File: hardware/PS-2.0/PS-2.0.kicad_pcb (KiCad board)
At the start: 2 copper layers, 119.7 x 199.4 mm, 50 parts, among them J1 PinSocket_02x16_P2.54mm_Verti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, J2 Conn_01x05, J3 Conn_01x05, J8 Conn_01x03, J9 Conn_01x03, K1 RAYEX-L90, K2 RAYEX-L90, Q1 IRFPE50, Q2 IRFPE50, Q3 IRFPE50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

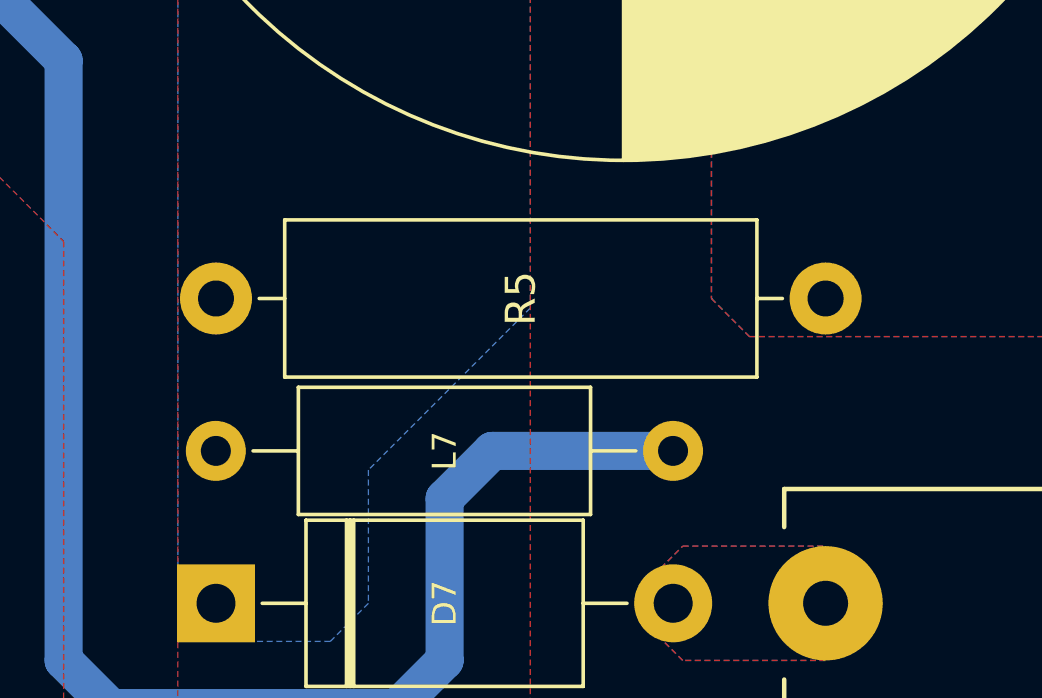
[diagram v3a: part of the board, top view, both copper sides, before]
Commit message: modified:   .DS_Store 	modified:   README.md 	deleted:    hardware/CTL-1.0/CTL-1.0-backups/CTL-1.0-2025-05-23_140814.zip 	deleted:    hardware/CTL-1.0/CTL-1.0-backups/CTL-1.0-2025-05-23_142136.zip 	deleted:    hardware/CTL-1.0/CTL-1.0-backups/CTL-1.0-2025-05-23_145207.zip 	deleted:    hardware/CTL-1.0/CTL-1.0-backups/CTL-1.0-2025-05-23_145749.zip 	deleted:    hardware/CTL-1.0/CTL-1.0-backups/CTL-1.0-2025-06-03_185115.zip 	new file:   hardware/CTL-1.0/CTL-1.0-backups/CTL-1.0-2025-06-04_091843.zip 	new file:   hardware/CTL-1.0/CTL-1.0-backups/CTL-1.0-2025-06-04_105408.zip 	new file:   hardware/CTL-1.0/CTL-1.0-backups/CTL-1.0-2025-06-04_105918.zip 	new file:   hardware/CTL-1.0/CTL-1.0-backups/CTL-1.0-2025-06-04_110436.zip 	new file:   hardware/CTL-1.0/CTL-1.0-backups/CTL-1.0-2025-06-04_115049.zip 	new file:   hardware/CTL-1.0/CTL-1.0-backups/CTL-1.0-2025-06-04_132910.zip 	modified:   hardware/CTL-1.0/CTL-1.0.kicad_pcb 	modified:   hardware/CTL-1.0/CTL-1.0.kicad_prl 	modified:   hardware/CTL-1.0/CTL-1.0.kicad_sch 	new file:   hardware/PS-2.0/PS-2.0-backups/PS-2.0-2025-06-04_100004.zip 	new file:   hardware/PS-2.0/PS-2.0-backups/PS-2.0-2025-06-04_102434.zip 	new file:   hardware/PS-2.0/PS-2.0-backups/PS-2.0-2025-06-04_104734.zip 	new file:   hardware/PS-2.0/PS-2.0-backups/PS-2.0-2025-06-04_133345.zip 	modified:   hardware/PS-2.0/PS-2.0.kicad_pcb 	modified:   hardware/PS-2.0/PS-2.0.kicad_prl 	modified:   hardware/PS-2.0/PS-2.0.kicad_sch 	new file:   hardware/PS-2.0/~PS-2.0.kicad_pcb.lck 	new file:   hardware/PS-2.0/~PS-2.0.kicad_sch.lck 	modified:   pic/.DS_Store 	new file:   pic/PWM/Wave-pure-cut-driver-mosfet.png 	renamed:    pic/PWM/blend-cut-1/blend-cut-1-10.csv -> pic/PWM/blend-cut-1/CTL/blend-cut-1-10.csv 	renamed:    pic/PWM/blend-cut-1/blend-cut-1-10.png -> pic/PWM/blend-cut-1/CTL/blend-cut-1-10.png 	renamed:    pic/PWM/blend-cut-1/blend-cut-1-100.csv -> pic/PWM/blend-cut-1/CTL/blend-cut-1-100.csv 	renamed:    pic/PWM/blend-cut-1/blend-cut-1-100.png -> pic/PWM/ble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
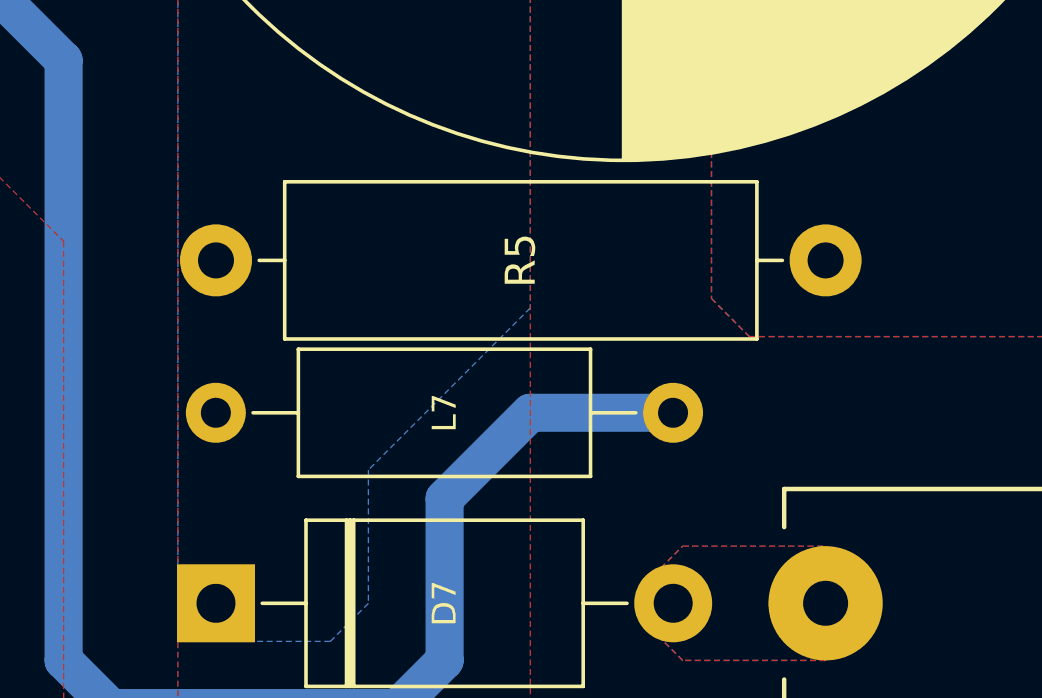
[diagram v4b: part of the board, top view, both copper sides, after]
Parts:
- moved L7 1.27 mm to (208.9, 190.5)
- moved R5 1.27 mm to (229.2, 185.4)
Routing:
- net Net-(C4-Pad1): track 186.0 -> 186.5 mm
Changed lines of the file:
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@@
 	(footprint "Inductor_THT:L_Axial_L9.5mm_D4.0mm_P15.24mm_Horizontal_Fastron_SMCC"
 		(layer "F.Cu")
-		(at 208.91 191.77)
+		(at 208.91 190.5)
 		(descr "Inductor, Axial series, Axial, Horizontal, pin pitch=15.24mm, , length*diameter=9.5*4mm^2, Fastron, SMCC, http://cdn-reichelt.de/documents/datenblatt/B400/DS_SMCC_NEU.pdf, http://cdn-reichelt.de/documents/datenblatt/B400/LEADEDINDUCTORS.pdf")
 		(tags "Inductor Axial series Axial Horizontal pin pitch 15.24mm  length 9.5mm diameter 4mm Fastron SMCC")
@@
 	(footprint "Resistor_THT:R_Axial_DIN0516_L15.5mm_D5.0mm_P20.32mm_Horizontal"
 		(layer "F.Cu")
-		(at 229.235 186.69 180)
+		(at 229.235 185.42 180)
 		(descr "Resistor, Axial_DIN0516 series, Axial, Horizontal, pin pitch=20.32mm, 2W, length*diameter=15.5*5mm^2, http://cdn-reichelt.de/documents/datenblatt/B400/1_4W%23YAG.pdf")
 		(tags "Resistor Axial_DIN0516 series Axial Horizontal pin pitch 20.32mm 2W length 15.5mm diameter 5mm")
@@
 	)
 	(segment
-		(start 205.4225 200.3425)
-		(end 203.835 198.755)
+		(start 216.535 198.755)
+		(end 214.9475 200.3425)
 		(width 1.27)
 		(layer "B.Cu")
@@
 	)
 	(segment
-		(start 196.5325 155.9325)
-		(end 199.7075 152.7575)
+		(start 168.335 126.0475)
+		(end 168.305 126.0775)
 		(width 1.27)
 		(layer "B.Cu")
@@
 	)
 	(segment
-		(start 168.335 126.0475)
-		(end 168.305 126.0775)
+		(start 203.835 178.7525)
+		(end 196.5325 171.45)
 		(width 1.27)
 		(layer "B.Cu")
@@
 	)
 	(segment
-		(start 218.1225 191.77)
-		(end 216.535 193.3575)
+		(start 205.4225 200.3425)
+		(end 203.835 198.755)
+		(width 1.27)
+		(layer "B.Cu")
+		(net 17)
+	)
+	(segment
+		(start 214.9475 200.3425)
+		(end 205.4225 200.3425)
 		(width 1.27)
 		(layer "B.Cu")
@@
 	)
 	(segment
-		(start 216.535 193.3575)
-		(end 216.535 198.755)
+		(start 196.5325 171.45)
+		(end 196.5325 155.9325)
 		(width 1.27)
 		(layer "B.Cu")
@@
 	)
 	(segment
-		(start 224.15 191.77)
-		(end 218.1225 191.77)
+		(start 216.535 193.3575)
+		(end 216.535 198.755)
+		(width 1.27)
+		(layer "B.Cu")
+		(net 17)
+	)
+	(segment
+		(start 196.5325 155.9325)
+		(end 199.7075 152.7575)
 		(width 1.27)
 		(layer "B.Cu")
@@
 	)
 	(segment
-		(start 203.835 198.755)
-		(end 203.835 178.7525)
+		(start 224.15 190.5)
+		(end 219.3925 190.5)
 		(width 1.27)
 		(layer "B.Cu")
@@
 	)
 	(segment
-		(start 214.9475 200.3425)
-		(end 205.4225 200.3425)
+		(start 219.3925 190.5)
+		(end 216.535 193.3575)
 		(width 1.27)
 		(layer "B.Cu")
@@
 	)
 	(segment
-		(start 203.835 178.7525)
-		(end 196.5325 171.45)
-		(width 1.27)
-		(layer "B.Cu")
-		(net 17)
-	)
-	(segment
 		(start 166.0025 100.5975)
 		(end 171.1325 105.7275)
@@
 	)
 	(segment
-		(start 166.0825 116.87)
-		(end 166.0825 123.855)
-		(width 1.778)
+		(start 203.835 198.755)
+		(end 203.835 178.7525)
+		(width 1.27)
 		(layer "B.Cu")
 		(net 17)
 	)
 	(segment
-		(start 196.5325 171.45)
-		(end 196.5325 155.9325)
-		(width 1.27)
+		(start 166.0825 116.87)
+		(end 166.0825 123.855)
+		(width 1.778)
 		(layer "B.Cu")
 		(net 17)
@@
 		(layer "B.Cu")
 		(net 17)
-	)
-	(segment
-		(start 216.535 198.755)
-		(end 214.9475 200.3425)
-		(width 1.27)
-		(layer "B.Cu")
-		(net 17)

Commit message: modified:   README.md 	deleted:    hardware/CTL-1.0/CTL-1.0-backups/CTL-1.0-2025-05-27_175205.zip 	deleted:    hardware/CTL-1.0/CTL-1.0-backups/CTL-1.0-2025-05-27_180035.zip 	deleted:    hardware/CTL-1.0/CTL-1.0-backups/CTL-1.0-2025-05-27_181441.zip 	deleted:    hardware/CTL-1.0/CTL-1.0-backups/CTL-1.0-2025-05-27_182529.zip 	deleted:    hardware/CTL-1.0/CTL-1.0-backups/CTL-1.0-2025-05-27_183819.zip 	deleted:    hardware/CTL-1.0/CTL-1.0-backups/CTL-1.0-2025-05-28_201558.zip 	deleted:    hardware/CTL-1.0/CTL-1.0-backups/CTL-1.0-2025-06-04_091843.zip 	new file:   hardware/CTL-1.0/CTL-1.0-backups/CTL-1.0-2025-06-05_141632.zip 	new file:   hardware/CTL-1.0/CTL-1.0-backups/CTL-1.0-2025-06-05_142549.zip 	new file:   hardware/CTL-1.0/CTL-1.0-backups/CTL-1.0-2025-06-05_143053.zip 	new file:   hardware/CTL-1.0/CTL-1.0-backups/CTL-1.0-2025-06-05_144242.zip 	new file:   hardware/CTL-1.0/CTL-1.0-backups/CTL-1.0-2025-06-05_144757.zip 	new file:   hardware/CTL-1.0/CTL-1.0-backups/CTL-1.0-2025-06-05_145506.zip 	modified:   hardware/CTL-1.0/CTL-1.0.kicad_pcb 	modified:   hardware/CTL-1.0/CTL-1.0.kicad_prl 	modified:   hardware/CTL-1.0/CTL-1.0.kicad_sch 	modified:   hardware/CTL-1.0/fp-info-cache 	new file:   hardware/PS-2.0/PS-2.0-backups/PS-2.0-2025-06-05_110653.zip 	new file:   hardware/PS-2.0/PS-2.0-backups/PS-2.0-2025-06-05_111332.zip 	new file:   hardware/PS-2.0/PS-2.0-backups/PS-2.0-2025-06-05_115228.zip 	new file:   hardware/PS-2.0/PS-2.0-backups/PS-2.0-2025-06-05_125334.zip 	modified:   hardware/PS-2.0/PS-2.0.kicad_pcb 	modified:   hardware/PS-2.0/PS-2.0.kicad_prl 	modified:   hardware/PS-2.0/PS-2.0.kicad_sch 	deleted:    hardware/PS-2.0/~PS-2.0.kicad_pcb.lck 	deleted:    hardware/PS-2.0/~PS-2.0.kicad_sch.lck 	modified:   pic/.DS_Store
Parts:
- J8, J9: value Conn_01x03 -> Conn_01x02
- R5: value 120Ω 2W -> 10kΩ 3W
- moved J9 0.19 mm to (126.4, 106.0)
- moved J8 0.19 mm to (126.4, 77.2)
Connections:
- net Net-(J1-Pin_10) renamed /OPTO
- net Net-(J1-Pin_5) renamed /+5V
- net Net-(J1-Pin_7) renamed /MSD1
- net Net-(J1-Pin_8) renamed /MSD2
- net Net-(J1-Pin_9) renamed /REM
- J1 pad 6: Net-(J1-Pin_6) -> GND
- K1 pad 12: Net-(J9-Pin_1) -> Net-(J8-Pin_2)
- K1 pad 14: Net-(J9-Pin_3) -> Net-(J9-Pin_2)
- K2 pad 14: Net-(J8-Pin_3) -> Net-(J9-Pin_1)
- U2 pad 2: Net-(J1-Pin_6) -> GND
- U3 pad 2: Net-(J1-Pin_6) -> GND
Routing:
- net Net-(J1-Pin_6): track 110.5 -> 0.00 mm
- net GND: track 0.00 -> 110.5 mm
- net Net-(J8-Pin_2): track 0.00 -> 43.7 mm, vias 0 -> 1
- net Net-(J9-Pin_2): track 0.00 -> 42.9 mm
- net Net-(J8-Pin_3): track 42.9 -> 0.00 mm
- net Net-(J9-Pin_3): track 42.9 -> 0.00 mm
- net Net-(J9-Pin_1): track 29.6 -> 57.0 mm

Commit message: modified:   .DS_Store 	new file:   .~Ferrite Transformer Calculation.xlsx 	new file:   .~Voltage.xlsx 	new file:   Ferrite Transformer Calculation.xlsx 	modified:   README.md 	new file:   Voltage.xlsx 	modified:   firmware/ESP32-S3 PWM/src/main.cpp 	deleted:    hardware/CTL-1.0/CTL-1.0-backups/CTL-1.0-2025-05-28_202523.zip 	new file:   hardware/CTL-1.0/CTL-1.0-backups/CTL-1.0-2025-07-03_115731.zip 	new file:   hardware/PS-2.0/PS-2.0-backups/PS-2.0-2025-06-18_154635.zip 	new file:   hardware/PS-2.0/PS-2.0-backups/PS-2.0-2025-06-19_101754.zip 	modified:   hardware/PS-2.0/PS-2.0.kicad_pcb 	modified:   hardware/PS-2.0/PS-2.0.kicad_sch 	new file:   hardware/XF-1.0/XF-1.0-backups/XF-1.0-2025-06-19_140209.zip 	new file:   hardware/XF-1.0/XF-1.0-backups/XF-1.0-2025-06-19_140721.zip 	new file:   hardware/XF-1.0/XF-1.0-backups/XF-1.0-2025-06-19_141456.zip 	new file:   hardware/XF-1.0/XF-1.0-backups/XF-1.0-2025-06-19_142018.zip 	new file:   hardware/XF-1.0/XF-1.0-backups/XF-1.0-2025-06-19_142518.zip 	new file:   hardware/XF-1.0/XF-1.0-backups/XF-1.0-2025-06-28_090149.zip 	new file:   hardware/XF-1.0/XF-1.0-backups/XF-1.0-2025-07-03_112321.zip 	new file:   hardware/XF-1.0/XF-1.0-backups/XF-1.0-2025-07-14_112815.zip 	new file:   hardware/XF-1.0/XF-1.0.kicad_pcb 	new file:   hardware/XF-1.0/XF-1.0.kicad_prl 	new file:   hardware/XF-1.0/XF-1.0.kicad_pro 	new file:   hardware/XF-1.0/XF-1.0.kicad_sch 	new file:   hardware/XF-1.0/fp-info-cache 	renamed:    hardware/PS-2.0/~PS-2.0.kicad_sch.lck -> hardware/XF-1.0/~XF-1.0.kicad_pcb.lck 	new file:   hardware/XF-1.0/~XF-1.0.kicad_sch.lck 	modified:   log.md
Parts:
- moved D2 5.08 mm to (221.9, 84.1)
- moved D1 5.08 mm to (221.9, 122.2)
- moved D3 5.08 mm to (221.9, 46.0)
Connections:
- L2 pad 1: Net-(D1-K) -> Net-(Q1-D)
- L4 pad 1: Net-(D2-K) -> Net-(Q2-D)
- L6 pad 1: Net-(D3-K) -> Net-(Q3-D)
- Q1 pad 1: Net-(Q1-G) -> Net-(D1-K)
- Q1 pad 2: Net-(D1-K) -> Net-(Q1-D)
- Q2 pad 1: Net-(Q2-G) -> Net-(D2-K)
- Q2 pad 2: Net-(D2-K) -> Net-(Q2-D)
- Q3 pad 1: Net-(Q3-G) -> Net-(D3-K)
- Q3 pad 2: Net-(D3-K) -> Net-(Q3-D)
- R1 pad 1: Net-(Q1-G) -> Net-(D1-K)
- R2 pad 1: Net-(Q2-G) -> Net-(D2-K)
- R3 pad 1: Net-(Q3-G) -> Net-(D3-K)
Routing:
- net Net-(Q3-G): track 12.1 -> 0.00 mm
- net Net-(Q2-G): track 12.1 -> 0.00 mm
- net Net-(Q1-G): track 12.1 -> 0.00 mm
- net Net-(Q1-D): track 0.00 -> 12.1 mm
- net Net-(Q3-D): track 0.00 -> 12.1 mm
- net Net-(Q2-D): track 0.00 -> 12.1 mm
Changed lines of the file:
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@@
 	(net 1 "unconnected-(U1-NC-Pad3)")
 	(net 2 "VDD")
-	(net 3 "Net-(Q1-G)")
+	(net 3 "Net-(Q1-D)")
 	(net 4 "Net-(R1-Pad2)")
 	(net 5 "Net-(CR1-Pad2)")
-	(net 6 "Net-(Q2-G)")
-	(net 7 "Net-(Q3-G)")
+	(net 6 "Net-(Q2-D)")
+	(net 7 "Net-(Q3-D)")
 	(net 8 "Net-(D4-A)")
 	(net 9 "GND")
@@
 			(layers "*.Cu" "*.Mask")
 			(remove_unused_layers no)
-			(net 7 "Net-(Q3-G)")
+			(net 13 "Net-(D3-K)")
 			(pinfunction "G")
 			(pintype "input")
@@
 			(layers "*.Cu" "*.Mask")
 			(remove_unused_layers no)
-			(net 13 "Net-(D3-K)")
+			(net 7 "Net-(Q3-D)")
 			(pinfunction "D")
 			(pintype "passive")
@@
 			(layers "*.Cu" "*.Mask")
 			(remove_unused_layers no)
-			(net 3 "Net-(Q1-G)")
+			(net 11 "Net-(D1-K)")
 			(pinfunction "G")
 			(pintype "input")
@@
 			(layers "*.Cu" "*.Mask")
 			(remove_unused_layers no)
-			(net 11 "Net-(D1-K)")
+			(net 3 "Net-(Q1-D)")
 			(pinfunction "D")
 			(pintype "passive")
@@
 	(footprint "Diode_THT:D_DO-41_SOD81_P10.16mm_Horizontal"
 		(layer "F.Cu")
-		(at 221.9275 89.2175 -90)
+		(at 221.9325 84.1375 -90)
 		(descr "Diode, DO-41_SOD81 series, Axial, Horizontal, pin pitch=10.16mm, , length*diameter=5.2*2.7mm^2, , http://www.diodes.com/_files/packages/DO-41%20(Plastic).pdf")
 		(tags "Diode DO-41_SOD81 series Axial Horizontal pin pitch 10.16mm  length 5.2mm diameter 2.7mm")
@@
 			(layers "*.Cu" "*.Mask")
 			(remove_unused_layers no)
-			(net 3 "Net-(Q1-G)")
+			(net 11 "Net-(D1-K)")
 			(pintype "passive")
 		)
@@
 			(layers "*.Cu" "*.Mask")
 			(remove_unused_layers no)
-			(net 6 "Net-(Q2-G)")
+			(net 12 "Net-(D2-K)")
 			(pintype "passive")
 		)
@@
 	(footprint "Diode_THT:D_DO-41_SOD81_P10.16mm_Horizontal"
 		(layer "F.Cu")
-		(at 221.9325 127.3175 -90)
+		(at 221.9325 122.2375 -90)
 		(descr "Diode, DO-41_SOD81 series, Axial, Horizontal, pin pitch=10.16mm, , length*diameter=5.2*2.7mm^2, , http://www.diodes.com/_files/packages/DO-41%20(Plastic).pdf")
 		(tags "Diode DO-41_SOD81 series Axial Horizontal pin pitch 10.16mm  length 5.2mm diameter 2.7mm")
@@
 			(layers "*.Cu" "*.Mask")
 			(remove_unused_layers no)
-			(net 7 "Net-(Q3-G)")
+			(net 13 "Net-(D3-K)")
 			(pintype "passive")
 		)
@@
 			(layers "*.Cu" "*.Mask")
 			(remove_unused_layers no)
-			(net 12 "Net-(D2-K)")
+			(net 6 "Net-(Q2-D)")
 			(pinfunction "1")
 			(pintype "passive")
@@
 	(footprint "Diode_THT:D_DO-41_SOD81_P10.16mm_Horizontal"
 		(layer "F.Cu")
-		(at 221.9325 51.1175 -90)
+		(at 221.9325 46.0375 -90)
 		(descr "Diode, DO-41_SOD81 series, Axial, Horizontal, pin pitch=10.16mm, , length*diameter=5.2*2.7mm^2, , http://www.diodes.com/_files/packages/DO-41%20(Plastic).pdf")
 		(tags "Diode DO-41_SOD81 series Axial Horizontal pin pitch 10.16mm  length 5.2mm diameter 2.7mm")
@@
 			(layers "*.Cu" "*.Mask")
 			(remove_unused_layers no)
-			(net 13 "Net-(D3-K)")
+			(net 7 "Net-(Q3-D)")
 			(pinfunction "1")
 			(pintype "passive")
@@
 			(layers "*.Cu" "*.Mask")
 			(remove_unused_layers no)
-			(net 11 "Net-(D1-K)")
+			(net 3 "Net-(Q1-D)")
 			(pinfunction "1")
 			(pintype "passive")
@@
 			(layers "*.Cu" "*.Mask")
 			(remove_unused_layers no)
-			(net 6 "Net-(Q2-G)")
+			(net 12 "Net-(D2-K)")
 			(pinfunction "G")
 			(pintype "input")
@@
 			(layers "*.Cu" "*.Mask")
 			(remove_unused_layers no)
-			(net 12 "Net-(D2-K)")
+			(net 6 "Net-(Q2-D)")
 			(pinfunction "D")
 			(pintype "passive")
@@
 		(end 139.3825 106.045)
 		(stroke
-			(width 0)
+			(width 0.1)
 			(type default)
 		)
@@
 	)
 	(segment
-		(start 228.23 121.92)
-		(end 228.2825 121.8675)
+		(start 221.9325 127.3175)
+		(end 228.2825 127.3175)
 		(width 1.778)
 		(layer "B.Cu")
@@
 	)
 	(segment
-		(start 216.2175 121.92)
-		(end 228.23 121.92)
+		(start 216.2175 127.3175)
+		(end 221.9325 127.3175)
 		(width 1.778)
 		(layer "B.Cu")
@@
 	)
 	(segment
-		(start 228.225 83.82)
-		(end 228.2775 83.7675)
+		(start 216.2175 89.2175)
+		(end 221.9275 89.2175)
 		(width 1.778)
 		(layer "B.Cu")
@@
 	)
 	(segment
-		(start 216.2125 83.82)
-		(end 228.225 83.82)
+		(start 221.9275 89.2175)
+		(end 228.2775 89.2175)
 		(width 1.778)
 		(layer "B.Cu")
@@
 	)
 	(segment
-		(start 228.23 45.72)
-		(end 228.2825 45.6675)
+		(start 216.2225 51.1175)
+		(end 221.9325 51.1175)
 		(width 1.778)
 		(layer "B.Cu")
@@
 	)
 	(segment
-		(start 216.2175 45.72)
-		(end 228.23 45.72)
+		(start 221.9325 51.1175)
+		(end 228.2825 51.1175)
 		(width 1.778)
 		(layer "B.Cu")
@@
 	)
 	(segment
-		(start 221.9325 127.3175)
-		(end 228.2825 127.3175)
+		(start 228.23 121.92)
+		(end 228.2825 121.8675)
 		(width 1.778)
 		(layer "B.Cu")
@@
 	)
 	(segment
-		(start 216.2175 127.3175)
-		(end 221.9325 127.3175)
+		(start 216.2175 121.92)
+		(end 228.23 121.92)
 		(width 1.778)
 		(layer "B.Cu")
@@
 	)
 	(segment
-		(start 216.2175 89.2175)
-		(end 221.9275 89.2175)
+		(start 228.225 83.82)
+		(end 228.2775 83.7675)
 		(width 1.778)
 		(layer "B.Cu")
@@
 	)
 	(segment
-		(start 221.9275 89.2175)
-		(end 228.2775 89.2175)
+		(start 216.2125 83.82)
+		(end 228.225 83.82)
 		(width 1.778)
 		(layer "B.Cu")
@@
 	)
 	(segment
-		(start 216.2225 51.1175)
-		(end 221.9325 51.1175)
+		(start 228.23 45.72)
+		(end 228.2825 45.6675)
 		(width 1.778)
 		(layer "B.Cu")
@@
 	)
 	(segment
-		(start 221.9325 51.1175)
-		(end 228.2825 51.1175)
+		(start 216.2175 45.72)
+		(end 228.23 45.72)
 		(width 1.778)
 		(layer "B.Cu")

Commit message: modified:   README.md 	deleted:    hardware/CTL-1.0/CTL-1.0-backups/CTL-1.0-2025-05-28_203806.zip 	deleted:    hardware/CTL-1.0/CTL-1.0-backups/CTL-1.0-2025-05-28_204313.zip 	deleted:    hardware/CTL-1.0/CTL-1.0-backups/CTL-1.0-2025-05-30_173028.zip 	deleted:    hardware/CTL-1.0/CTL-1.0-backups/CTL-1.0-2025-05-30_174116.zip 	deleted:    hardware/CTL-1.0/CTL-1.0-backups/CTL-1.0-2025-05-30_175122.zip 	new file:   hardware/CTL-1.0/CTL-1.0-backups/CTL-1.0-2025-07-24_151142.zip 	new file:   hardware/CTL-1.0/CTL-1.0-backups/CTL-1.0-2025-07-24_172002.zip 	new file:   hardware/CTL-1.0/CTL-1.0-backups/CTL-1.0-2025-07-25_175122.zip 	new file:   hardware/CTL-1.0/CTL-1.0-backups/CTL-1.0-2025-07-26_120011.zip 	new file:   hardware/CTL-1.0/CTL-1.0-backups/CTL-1.0-2025-07-26_120808.zip 	modified:   hardware/CTL-1.0/CTL-1.0.kicad_pcb 	modified:   hardware/CTL-1.0/CTL-1.0.kicad_pro 	new file:   hardware/CTL-1.0/CTL-1.0.step 	deleted:    hardware/MSD-1.0/MSD-1.0-backups/MSD-1.0-2025-04-11_111943.zip 	deleted:    hardware/MSD-1.0/MSD-1.0-backups/MSD-1.0-2025-04-11_113401.zip 	new file:   hardware/MSD-1.0/MSD-1.0-backups/MSD-1.0-2025-07-25_163151.zip 	new file:   hardware/MSD-1.0/MSD-1.0-backups/MSD-1.0-2025-07-25_171843.zip 	modified:   hardware/MSD-1.0/MSD-1.0.kicad_pcb 	modified:   hardware/MSD-1.0/MSD-1.0.step 	new file:   hardware/MSD-1.1/MSD-1.1-backups/MSD-1.1-2025-07-24_151252.zip 	new file:   hardware/MSD-1.1/MSD-1.1-backups/MSD-1.1-2025-07-25_152939.zip 	new file:   hardware/MSD-1.1/MSD-1.1-backups/MSD-1.1-2025-07-25_162346.zip 	new file:   hardware/MSD-1.1/MSD-1.1-backups/MSD-1.1-2025-07-25_162917.zip 	modified:   hardware/MSD-1.1/MSD-1.1.kicad_pcb 	modified:   hardware/MSD-1.1/MSD-1.1.step 	modified:   hardware/MSD-1.1/fp-info-cache 	new file:   hardware/MSD-2.0/MSD-2.0-backups/MSD-2.0-2025-07-24_151230.zip 	deleted:    hardware/PS-2.0/PS-2.0-backups/PS-2.0-2025-05-07_010425.zip 	deleted:    hardware/PS-2.0/PS-2.0-backups/PS-2.0-2025-05-09_084820.zip 	deleted:    hardware/P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
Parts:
- added H5: MountingHole_Pad, MountingHole:MountingHole_3.2mm_M3_ISO14580_Pad, F.Cu at (126.7, 114.6)
- added H6: MountingHole_Pad, MountingHole:MountingHole_3.2mm_M3_ISO14580_Pad, F.Cu at (216.2, 114.6)
- moved J9 10.2 mm to (126.4, 95.9)
- moved J1 3.81 mm to (194.6, 186.7)
- moved U3 3.81 mm to (179.4, 128.9)
- moved U2 2.54 mm to (148.9, 128.9)
- moved D8 0.67 mm to (187.6, 109.9)
- moved D9 0.66 mm to (187.6, 81.0)
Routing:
- net /RLY-K: track 155.2 -> 142.5 mm
- net Net-(J3-Pin_5): track 90.1 -> 78.7 mm
- net Net-(J9-Pin_1): track 57.0 -> 47.4 mm
- net /REM: track 107.9 -> 99.9 mm
- net /+5V: track 111.1 -> 103.5 mm
- net GND: track 110.5 -> 103.5 mm
- net Net-(J9-Pin_2): track 42.9 -> 47.1 mm
- net /OPTO: track 7.62 -> 11.4 mm
- net Net-(J3-Pin_3): track 84.6 -> 80.8 mm
- net Net-(J3-Pin_1): track 87.5 -> 83.8 mm
- net /RLY-A: track 132.2 -> 128.9 mm
- net /MSD2: track 77.3 -> 74.0 mm
- net /MSD1: track 78.4 -> 75.3 mm
- net /PWM: track 54.7 -> 51.9 mm
- net Net-(J2-Pin_3): track 28.2 -> 25.6 mm
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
